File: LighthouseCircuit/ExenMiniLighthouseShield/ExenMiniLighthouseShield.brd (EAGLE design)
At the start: 25.4 x 11.4 mm, 23 parts

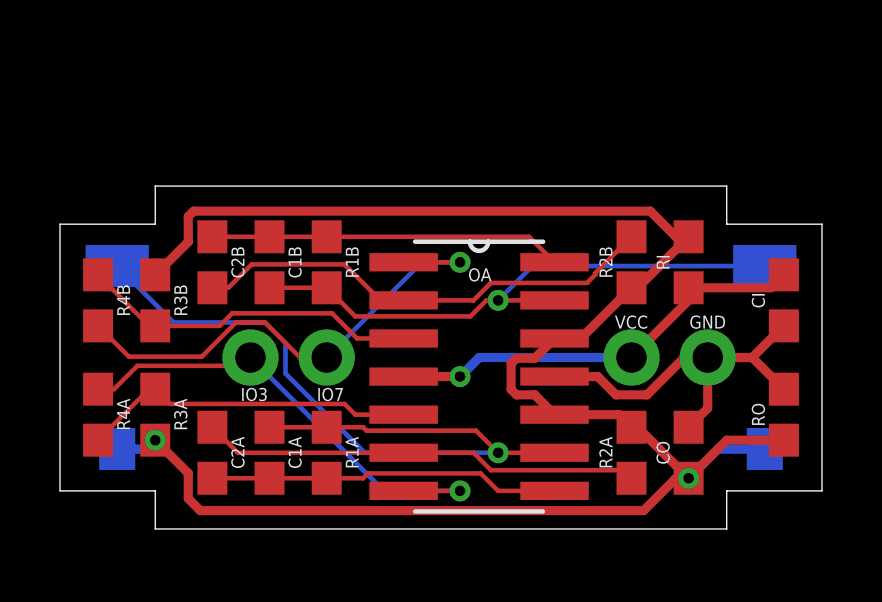
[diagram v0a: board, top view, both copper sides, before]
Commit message: Moved to separate PID configuration for each wheel. Since the left wheel is offset toward the rear and the right wheel is offset toward the front, the left wheel needs to be less aggressive or the Zippy will turn more quickly to the right and will tilt the robot and pull the right wheel off the ground, preventing contact with the floor. On the other hand, the right wheel needs to be more aggressive or turns to the left will be slower than turns to the right.
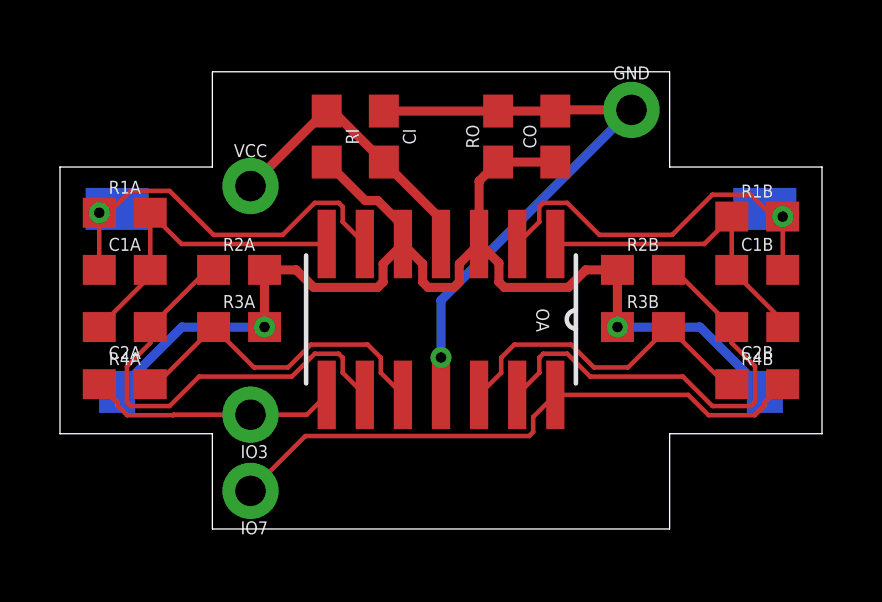
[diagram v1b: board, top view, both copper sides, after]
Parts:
- C1A, C1B: value 5pF -> 2.2pF
- GND: value (none) -> SINGLE-THROUGH-HOLE; device SparkFun-Connectors:1X01_NO_SILK -> ZippyComponentLibrary:SINGLE-THROUGH-HOLE
- R1A, R1B: value 120k -> 100k
- moved R4B 22.1 mm to (23.2, 4.83), turned to 0 degrees
- moved C2B 18.3 mm to (23.2, 6.73), turned to 180 degrees
- moved R3B 16.3 mm to (19.4, 6.73), turned to 180 degrees
- moved C1B 16.3 mm to (23.2, 8.64), turned to 180 degrees
- moved R1B 14.4 mm to (23.2, 10.4), turned to 180 degrees
- moved R2A 14.4 mm to (5.97, 8.64), turned to 0 degrees
- moved CI 14.4 mm to (10.8, 13.1), turned to 90 degrees
- moved VCC 13.9 mm to (6.35, 11.4)
- moved RO 13.3 mm to (14.6, 13.1)
- moved RI 12.8 mm to (8.89, 13.1), turned to 90 degrees
- moved CO 11.4 mm to (16.5, 13.1)
- moved R1A 10.5 mm to (2.16, 10.5), turned to 0 degrees
- moved GND 8.64 mm to (19.1, 14.0)
- moved C1A 7.78 mm to (2.16, 8.64), turned to 0 degrees
- moved IO7 5.12 mm to (6.35, 1.27)
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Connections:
- net D1IN: now also OA.2; no longer OA.13
- net D1OA2P: now also OA.13; no longer OA.2
- net D1OAOUT1: now also OA.1; no longer OA.14
- net D2IN: now also OA.6; no longer OA.9
- net D2OA1OUT: now also OA.7; no longer OA.8
- net D2OA2N: now also OA.10; no longer OA.5
- net D2OA2P: now also OA.9; no longer OA.6
- net IO3: now also OA.8; no longer OA.7
- net IO7: now also OA.14; no longer OA.1
- net LVCC: now also OA.3, OA.5; no longer OA.10, OA.12
- net N$11: now also OA.12; no longer OA.3
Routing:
- net LVCC: track 62.9 -> 40.5 mm
- net D2IN: track 25.7 -> 13.6 mm
- net IO3: track 16.2 -> 8.35 mm, vias 1 -> 0
- net GND: track 12.9 -> 20.4 mm, vias 0 -> 1
- net D1IN: track 19.5 -> 13.5 mm
- net VCC: track 14.3 -> 9.71 mm, vias 1 -> 0
- net IO7: track 16.6 -> 20.1 mm, vias 1 -> 0
- net D1OAOUT1: track 11.8 -> 10.6 mm
- net D2OA1OUT: track 11.7 -> 10.8 mm
- net D2OA2P: track 14.7 -> 15.3 mm
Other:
- board size 25.4 x 11.4 mm -> 25.4 x 15.2 mm

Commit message: Reached a point where auto-drive mode is consistent and reliable.
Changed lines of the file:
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@@
 <wire x1="0" y1="3.175" x2="5.08" y2="3.175" width="0" layer="20"/>
 <wire x1="5.08" y1="3.175" x2="5.08" y2="0" width="0" layer="20"/>
-<text x="12.065" y="0.635" size="0.6096" layer="22" font="vector" ratio="7" rot="MR90">Designed, Manufactured, and
+<text x="8.255" y="0.635" size="0.6096" layer="22" font="vector" ratio="7" rot="MR90">Designed, Manufactured, and
 Assembled by Kyle Davis</text>
 </plain>
@@
 <elements>
 <element name="VCC" library="SparkFun-Connectors" package="1X01_NO_SILK" value="" x="6.35" y="11.43" smashed="yes">
-<attribute name="NAME" x="6.35" y="12.827" size="0.4318" layer="25" font="vector" align="top-center"/>
+<attribute name="NAME" x="6.35" y="12.954" size="0.4318" layer="25" font="vector" align="top-center"/>
 <attribute name="VALUE" x="5.08" y="9.906" size="0.6096" layer="27" font="vector" ratio="20" align="top-left"/>
 </element>
@@
 </element>
 <element name="C2A" library="ZippyComponentLibrary" package="PASSIVE-0603" value="4.7nF" x="2.159" y="6.731" smashed="yes">
-<attribute name="NAME" x="2.159" y="6.096" size="0.4318" layer="25" font="vector" rot="R180" align="bottom-center"/>
+<attribute name="NAME" x="2.159" y="7.366" size="0.4318" layer="25" font="vector" align="bottom-center"/>
 </element>
 <element name="R1B" library="ZippyComponentLibrary" package="PASSIVE-0603" value="100k" x="23.241" y="10.414" smashed="yes" rot="R180">
@@
 </element>
 <element name="C2B" library="ZippyComponentLibrary" package="PASSIVE-0603" value="4.7nF" x="23.241" y="6.731" smashed="yes" rot="R180">
-<attribute name="NAME" x="23.241" y="6.096" size="0.4318" layer="25" font="vector" rot="R180" align="bottom-center"/>
+<attribute name="NAME" x="23.241" y="7.366" size="0.4318" layer="25" font="vector" align="bottom-center"/>
 </element>
 <element name="R2B" library="ZippyComponentLibrary" package="PASSIVE-0603" value="18k" x="19.431" y="8.636" smashed="yes" rot="R180">
@@
 <element name="D1" library="ZippyComponentLibrary" package="BPW34_BP104_SMD" value="PHOTODIODEBPW" x="1.905" y="7.62" rot="MR90"/>
 <element name="GND" library="ZippyComponentLibrary" package="SINGLE-THROUGH-HOLE" value="SINGLE-THROUGH-HOLE" x="19.05" y="13.97" smashed="yes">
-<attribute name="NAME" x="19.05" y="14.986" size="0.4318" layer="25" font="vector" align="bottom-center"/>
+<attribute name="NAME" x="19.05" y="12.446" size="0.4318" layer="25" font="vector" align="bottom-center"/>
 </element>
 </elements>
